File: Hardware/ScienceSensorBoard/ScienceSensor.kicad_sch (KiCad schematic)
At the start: 93 parts, among them J1 Conn_02x03_Counter_Clockwise, J2 RJ45_LED_Shielded, Q1 SI4156DY, Q10 BSS138, Q11 SI4156DY, Q2 SI4156DY, Q3 SI4156DY, Q4 BSS138, Q5 BSS138, Q6 BSS138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

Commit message: Unsaved changes
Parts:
- Conn10: footprint MRDT_Connectors:MOLEX_SL_05_Vertical -> MRDT_Connectors:MOLEX_SL_05_Horizontal
- Conn11, Conn13, Conn7, Conn8, Conn9: footprint MRDT_Connectors:MOLEX_SL_04_Vertical -> MRDT_Connectors:MOLEX_SL_04_Horizontal
- Conn12, Conn6: footprint MRDT_Connectors:MOLEX_SL_03_Vertical -> MRDT_Connectors:MOLEX_SL_03_Horizontal
- Conn3: footprint MRDT_Connectors:MOLEX_SL_02_Vertical -> MRDT_Connectors:MOLEX_SL_02_Horizontal
- Conn4: footprint MRDT_Connectors:MOLEX_SL_07_Vertical -> MRDT_Connectors:MOLEX_SL_07_Horizontal
- U3: footprint MODULE_DEV-16771 -> MRDT_Shields:Teensy_4_1_Vertical
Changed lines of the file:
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@@
       (effects (font (size 1.524 1.524)) (justify left))
     )
-    (property "Footprint" "MRDT_Connectors:MOLEX_SL_04_Vertical" (id 2) (at 238.76 41.91 0)
+    (property "Footprint" "MRDT_Connectors:MOLEX_SL_04_Horizontal" (id 2) (at 238.76 41.91 0)
       (effects (font (size 1.524 1.524)) hide)
     )
@@
       (effects (font (size 1.524 1.524)) (justify left))
     )
-    (property "Footprint" "MRDT_Connectors:MOLEX_SL_07_Vertical" (id 2) (at 302.26 31.115 0)
+    (property "Footprint" "MRDT_Connectors:MOLEX_SL_07_Horizontal" (id 2) (at 302.26 31.115 0)
       (effects (font (size 1.524 1.524)) hide)
     )
@@
     (property "Reference" "U3" (id 0) (at 57.785 172.2882 0))
     (property "Value" "Teensy4.1_DEV-16771" (id 1) (at 57.785 174.5996 0))
-    (property "Footprint" "MODULE_DEV-16771" (id 2) (at 111.125 234.95 0)
+    (property "Footprint" "MRDT_Shields:Teensy_4_1_Vertical" (id 2) (at 111.125 234.95 0)
       (effects (font (size 1.27 1.27)) (justify left bottom) hide)
     )
@@
       (effects (font (size 1.524 1.524)) (justify left))
     )
-    (property "Footprint" "MRDT_Connectors:MOLEX_SL_04_Vertical" (id 2) (at 372.745 146.05 0)
+    (property "Footprint" "MRDT_Connectors:MOLEX_SL_04_Horizontal" (id 2) (at 372.745 146.05 0)
       (effects (font (size 1.524 1.524)) hide)
     )
@@
       (effects (font (size 1.524 1.524)) (justify left) hide)
     )
-    (property "Footprint" "MRDT_Connectors:MOLEX_SL_02_Vertical" (id 2) (at 139.065 46.99 0)
+    (property "Footprint" "MRDT_Connectors:MOLEX_SL_02_Horizontal" (id 2) (at 139.065 46.99 0)
       (effects (font (size 1.524 1.524)) hide)
     )
@@
       (effects (font (size 1.524 1.524)) (justify left))
     )
-    (property "Footprint" "MRDT_Connectors:MOLEX_SL_03_Vertical" (id 2) (at 126.365 78.105 0)
+    (property "Footprint" "MRDT_Connectors:MOLEX_SL_03_Horizontal" (id 2) (at 126.365 78.105 0)
       (effects (font (size 1.524 1.524)) hide)
     )
@@
       (effects (font (size 1.524 1.524)) (justify left))
     )
-    (property "Footprint" "MRDT_Connectors:MOLEX_SL_04_Vertical" (id 2) (at 374.65 80.645 0)
+    (property "Footprint" "MRDT_Connectors:MOLEX_SL_04_Horizontal" (id 2) (at 374.65 80.645 0)
       (effects (font (size 1.524 1.524)) hide)
     )
@@
       (effects (font (size 1.524 1.524)) (justify left))
     )
-    (property "Footprint" "MRDT_Connectors:MOLEX_SL_04_Vertical" (id 2) (at 372.745 185.42 0)
+    (property "Footprint" "MRDT_Connectors:MOLEX_SL_04_Horizontal" (id 2) (at 372.745 185.42 0)
       (effects (font (size 1.524 1.524)) hide)
     )
@@
       (effects (font (size 1.524 1.524)) (justify left))
     )
-    (property "Footprint" "MRDT_Connectors:MOLEX_SL_04_Vertical" (id 2) (at 375.92 47.625 0)
+    (property "Footprint" "MRDT_Connectors:MOLEX_SL_04_Horizontal" (id 2) (at 375.92 47.625 0)
       (effects (font (size 1.524 1.524)) hide)
     )
@@
       (effects (font (size 1.524 1.524)) (justify left))
     )
-    (property "Footprint" "MRDT_Connectors:MOLEX_SL_05_Vertical" (id 2) (at 376.555 122.555 0)
+    (property "Footprint" "MRDT_Connectors:MOLEX_SL_05_Horizontal" (id 2) (at 376.555 122.555 0)
       (effects (font (size 1.524 1.524)) hide)
     )
@@
       (effects (font (size 1.524 1.524)) (justify left))
     )
-    (property "Footprint" "MRDT_Connectors:MOLEX_SL_03_Vertical" (id 2) (at 148.59 26.67 0)
+    (property "Footprint" "MRDT_Connectors:MOLEX_SL_03_Horizontal" (id 2) (at 148.59 26.67 0)
       (effects (font (size 1.524 1.524)) hide)
     )
@@
     )
     (path "/362043ba-7077-4355-842f-ed4e21c764a7"
-      (reference "Conn3") (unit 1) (value "Molex_SL_02") (footprint "MRDT_Connectors:MOLEX_SL_02_Vertical")
+      (reference "Conn3") (unit 1) (value "Molex_SL_02") (footprint "MRDT_Connectors:MOLEX_SL_02_Horizontal")
     )
     (path "/2cca1221-a56d-46b9-abdb-f313a2558695"
-      (reference "Conn4") (unit 1) (value "Molex_SL_07") (footprint "MRDT_Connectors:MOLEX_SL_07_Vertical")
+      (reference "Conn4") (unit 1) (value "Molex_SL_07") (footprint "MRDT_Connectors:MOLEX_SL_07_Horizontal")
     )
     (path "/726f2370-5511-4905-9eb4-028092273805"
@@
     )
     (path "/514d1d3a-5e7e-4cdf-800d-dc9fd4979572"
-      (reference "Conn6") (unit 1) (value "Molex_SL_03") (footprint "MRDT_Connectors:MOLEX_SL_03_Vertical")
+      (reference "Conn6") (unit 1) (value "Molex_SL_03") (footprint "MRDT_Connectors:MOLEX_SL_03_Horizontal")
     )
     (path "/17bdc4af-b7fd-461e-b9eb-6fab69389ac2"
-      (reference "Conn7") (unit 1) (value "Molex_SL_04") (footprint "MRDT_Connectors:MOLEX_SL_04_Vertical")
+      (reference "Conn7") (unit 1) (value "Molex_SL_04") (footprint "MRDT_Connectors:MOLEX_SL_04_Horizontal")
     )
     (path "/6a2e2e5d-609f-433a-995e-8e1ddb8bf56f"
-      (reference "Conn8") (unit 1) (value "Molex_SL_04") (footprint "MRDT_Connectors:MOLEX_SL_04_Vertical")
+      (reference "Conn8") (unit 1) (value "Molex_SL_04") (footprint "MRDT_Connectors:MOLEX_SL_04_Horizontal")
     )
     (path "/827787cb-a94a-4130-8cd6-2c43af0976f9"
-      (reference "Conn9") (unit 1) (value "Molex_SL_04") (footprint "MRDT_Connectors:MOLEX_SL_04_Vertical")
+      (reference "Conn9") (unit 1) (value "Molex_SL_04") (footprint "MRDT_Connectors:MOLEX_SL_04_Horizontal")
     )
     (path "/c5c8c731-d752-4329-b481-00d81fff6183"
-      (reference "Conn10") (unit 1) (value "Molex_SL_05") (footprint "MRDT_Connectors:MOLEX_SL_05_Vertical")
+      (reference "Conn10") (unit 1) (value "Molex_SL_05") (footprint "MRDT_Connectors:MOLEX_SL_05_Horizontal")
     )
     (path "/2fc579ad-59f7-42ce-8923-2fdbb5dabf35"
-      (reference "Conn11") (unit 1) (value "Molex_SL_04") (footprint "MRDT_Connectors:MOLEX_SL_04_Vertical")
+      (reference "Conn11") (unit 1) (value "Molex_SL_04") (footprint "MRDT_Connectors:MOLEX_SL_04_Horizontal")
     )
     (path "/c7884a03-c37f-45a7-baa0-a34c76a7670d"
-      (reference "Conn12") (unit 1) (value "Molex_SL_03") (footprint "MRDT_Connectors:MOLEX_SL_03_Vertical")
+      (reference "Conn12") (unit 1) (value "Molex_SL_03") (footprint "MRDT_Connectors:MOLEX_SL_03_Horizontal")
     )
     (path "/6e4603fe-e079-4657-9b84-fcd8115a1681"
-      (reference "Conn13") (unit 1) (value "Molex_SL_04") (footprint "MRDT_Connectors:MOLEX_SL_04_Vertical")
+      (reference "Conn13") (unit 1) (value "Molex_SL_04") (footprint "MRDT_Connectors:MOLEX_SL_04_Horizontal")
     )
     (path "/00000000-0000-0000-0000-000063231caf"
@@
     )
     (path "/2f88ba76-d045-4569-93f2-5dcb53794496"
-      (reference "U3") (unit 1) (value "Teensy4.1_DEV-16771") (footprint "MODULE_DEV-16771")
+      (reference "U3") (unit 1) (value "Teensy4.1_DEV-16771") (footprint "MRDT_Shields:Teensy_4_1_Vertical")
     )
     (path "/7fbf8d97-dbc7-433a-881b-00f505779a8f"

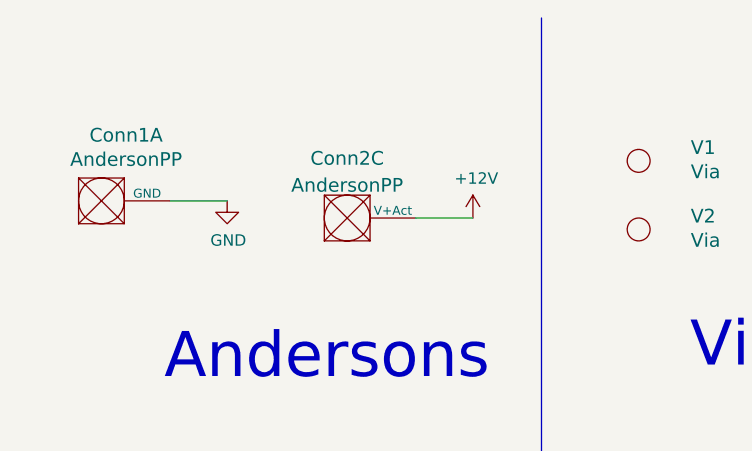
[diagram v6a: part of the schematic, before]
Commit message: Sensor Layout organization.
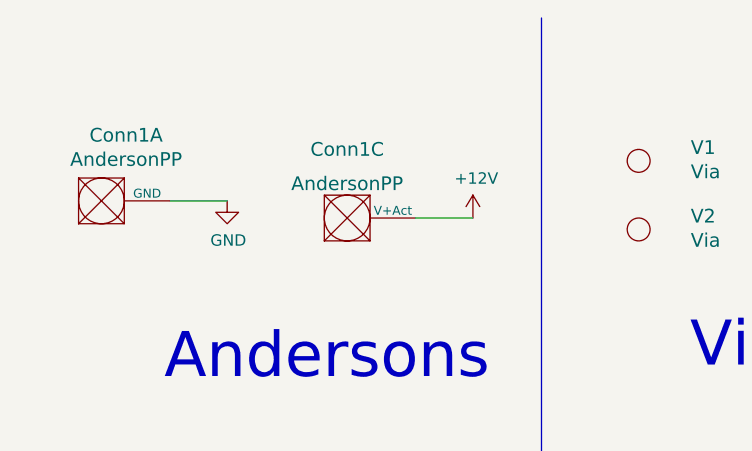
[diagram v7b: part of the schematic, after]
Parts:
- Conn10: footprint MRDT_Connectors:MOLEX_SL_05_Horizontal -> MRDT_Connectors:MOLEX_SL_05_Vertical
- Conn11, Conn13, Conn7, Conn8, Conn9: footprint MRDT_Connectors:MOLEX_SL_04_Horizontal -> MRDT_Connectors:MOLEX_SL_04_Vertical
- Conn12, Conn6: footprint MRDT_Connectors:MOLEX_SL_03_Horizontal -> MRDT_Connectors:MOLEX_SL_03_Vertical
- Conn3: footprint MRDT_Connectors:MOLEX_SL_02_Horizontal -> MRDT_Connectors:MOLEX_SL_02_Vertical
- Conn4: footprint MRDT_Connectors:MOLEX_SL_07_Horizontal -> MRDT_Connectors:MOLEX_SL_07_Vertical
- U2: footprint Converter_DCDC:Converter_DCDC_muRata_OKI-78SR_Horizontal -> MRDT_Devices:OKI_Horizontal
- U3: footprint MRDT_Shields:Teensy_4_1_Vertical -> MRDT_Shields:Teensy_4_1
- V1, V2, V3, V4: footprint MRDT_Drill_Holes:Via_.6mm -> MRDT_Drill_Holes:4_40_Hole
- renumbered Conn2 to Conn1

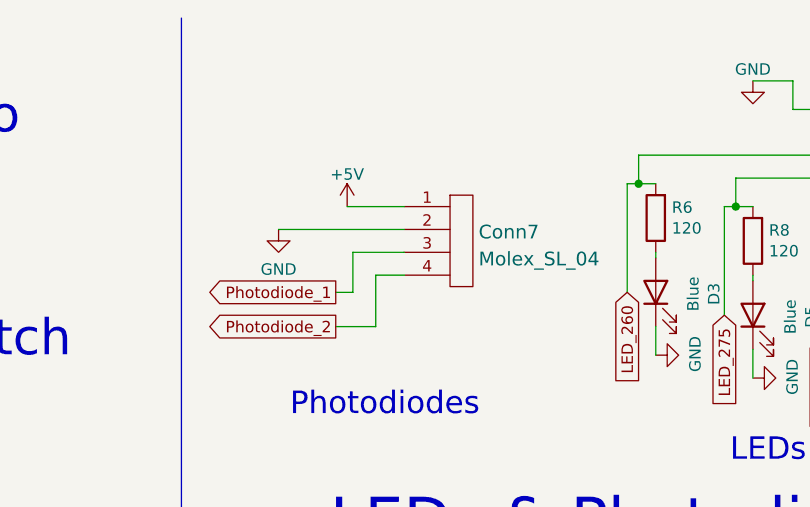
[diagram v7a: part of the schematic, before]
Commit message: Mosfets & H-Bridge Organized, Photodiode organized, Footprints for LED
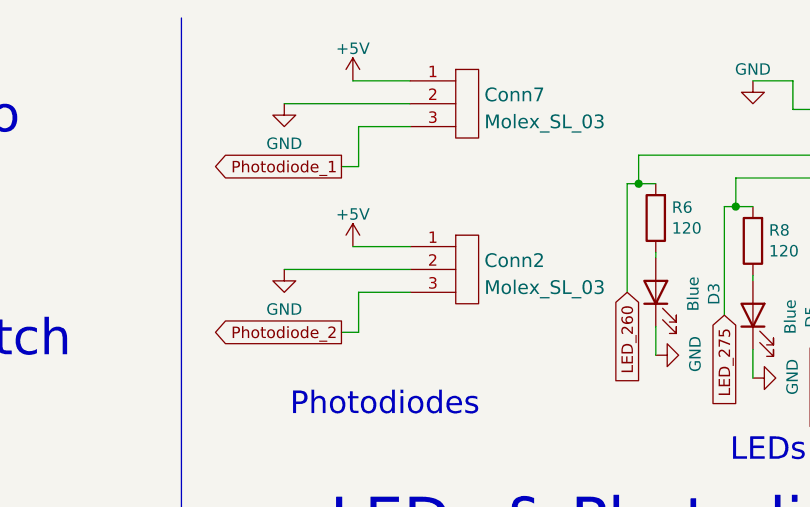
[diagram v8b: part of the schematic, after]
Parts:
- removed Conn7: Molex_SL_04, MRDT_Connectors:MOLEX_SL_04_Vertical, symbol MRDT_Connectors:Molex_SL_04
- added Conn2, Conn7: Molex_SL_03, MRDT_Connectors:MOLEX_SL_03_Horizontal, symbol MRDT_Connectors:Molex_SL_03
- Conn10: footprint MRDT_Connectors:MOLEX_SL_05_Vertical -> MRDT_Connectors:MOLEX_SL_05_Horizontal
- Conn11, Conn13, Conn8, Conn9: footprint MRDT_Connectors:MOLEX_SL_04_Vertical -> MRDT_Connectors:MOLEX_SL_04_Horizontal
- Conn12, Conn6: footprint MRDT_Connectors:MOLEX_SL_03_Vertical -> MRDT_Connectors:MOLEX_SL_03_Horizontal
- Conn3: footprint MRDT_Connectors:MOLEX_SL_02_Vertical -> MRDT_Connectors:MOLEX_SL_02_Horizontal
- Conn4: footprint MRDT_Connectors:MOLEX_SL_07_Vertical -> MRDT_Connectors:MOLEX_SL_07_Horizontal
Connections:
- net +5V: now also Conn2.1, Conn7.1
- net GND: now also Conn2.2, Conn7.2
- net Photodiode_1: now also Conn7.3
- net Photodiode_2: now also Conn2.3
